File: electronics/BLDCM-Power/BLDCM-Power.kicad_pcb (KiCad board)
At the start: 4 copper layers, 32 x 32 mm, 37 parts, among them J1 501920-3001, J2 53048-0310, J3 53261-0471, J4 53261-0471, J5 FTSH-107-01-L-DV-K, J6 12402012E212A, U1 INA239-Q1, U2 LDL212PV33R, U3 TMC6300-LA, U4 INA239-Q1, U5 TCAN1462, U6 INA239-Q1

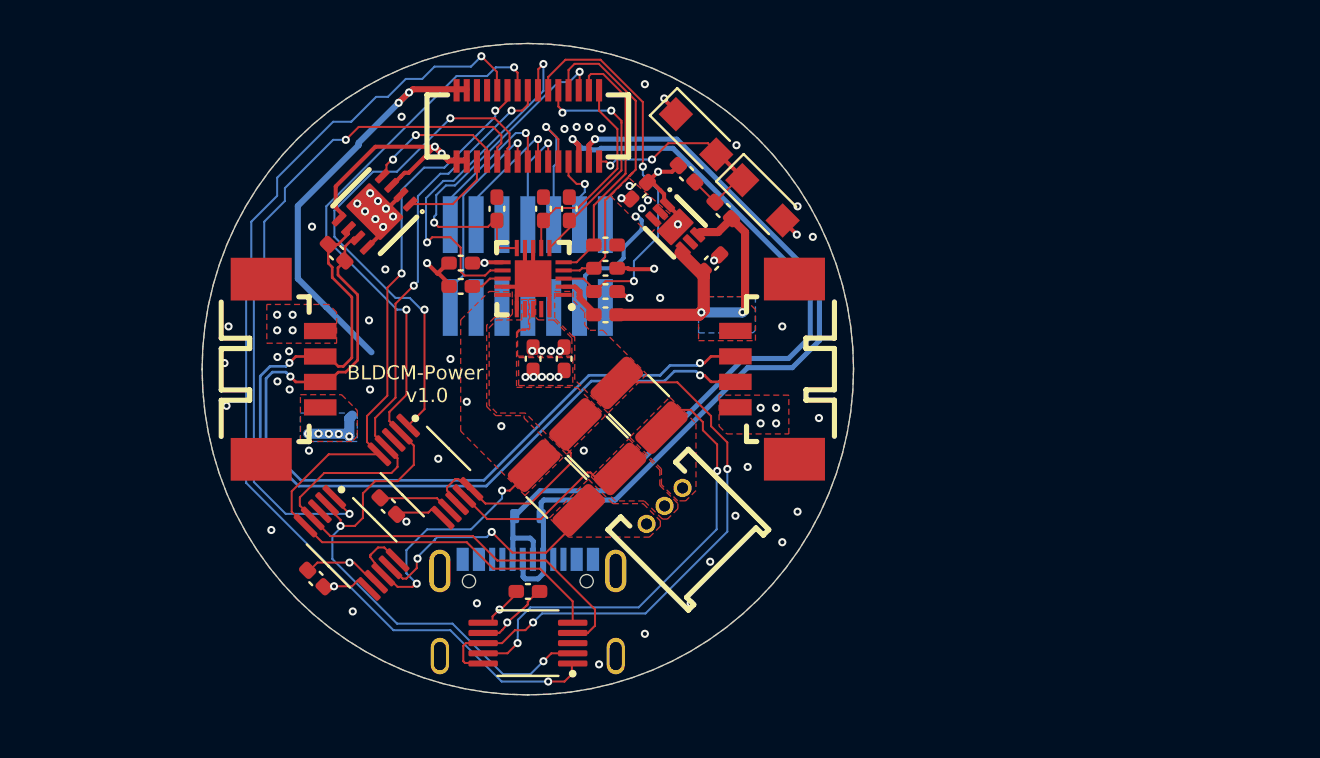
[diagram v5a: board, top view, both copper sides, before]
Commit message: Feat(schematic): Automatic power source selection
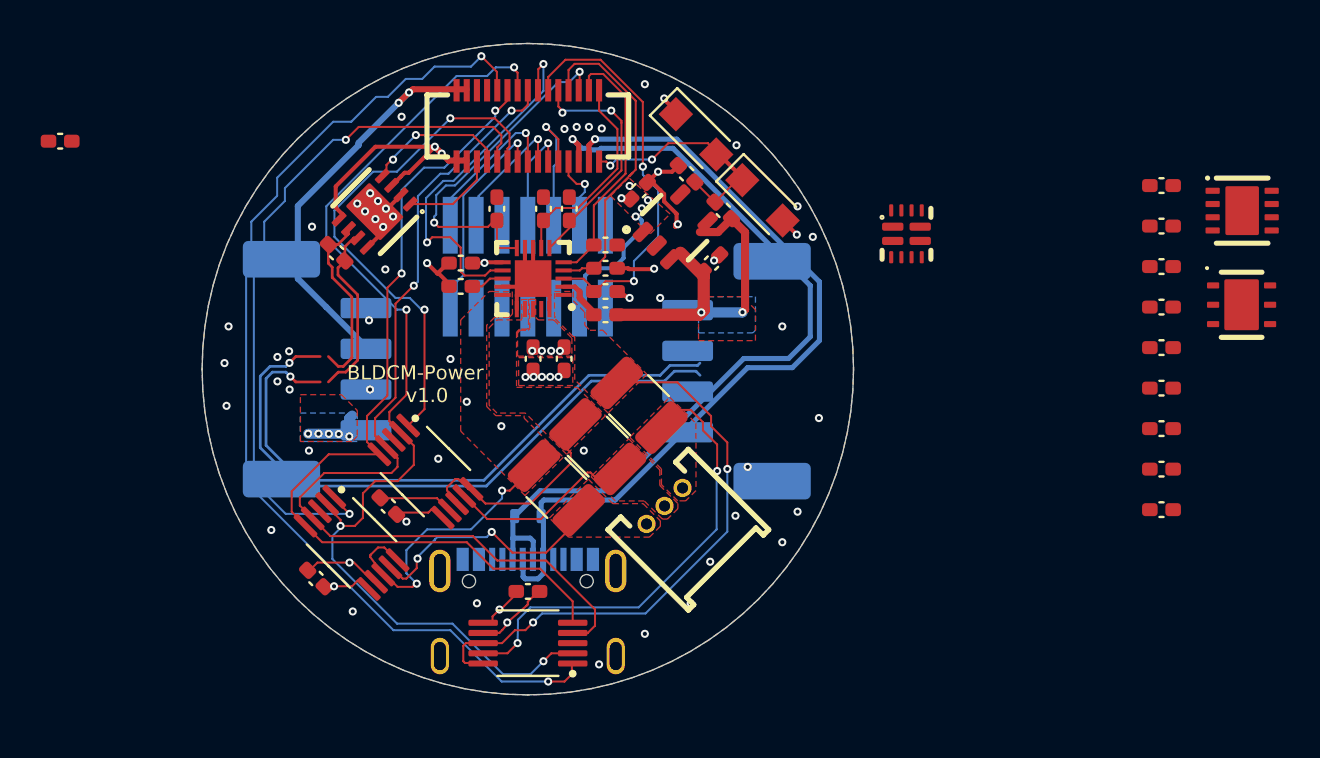
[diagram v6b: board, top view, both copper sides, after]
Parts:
- added C11: 1uF, BrenoCQ:C_0402, F.Cu at (179.6, 96.0)
- added C12: 1uF, BrenoCQ:C_0402, F.Cu at (179.6, 98.0)
- added C13: 100nF, BrenoCQ:C_0402, F.Cu at (179.6, 100.0)
- added C14: 100nF, BrenoCQ:C_0402, F.Cu at (179.6, 102.0)
- added R14: 100K, BrenoCQ:R_0402, F.Cu at (179.6, 103.9)
- added R15: 500, BrenoCQ:R_0402, F.Cu at (179.6, 105.9)
- added R16: 100K, BrenoCQ:R_0402, F.Cu at (179.6, 107.9)
- added R17: 100K, BrenoCQ:R_0402, F.Cu at (179.6, 109.9)
- added R18: 100K, BrenoCQ:R_0402, F.Cu at (179.6, 111.9)
- added R3: 5.1K, BrenoCQ:R_0402, F.Cu at (125.5, 93.8)
- added U7: TPS2121, BrenoCQ:VQFN-HR-12, F.Cu at (167.1, 98.4)
- added U8: LDO40LPU50RY, BrenoCQ:DFN-6-3x3, F.Cu at (183.6, 101.8)
- added U9: TPS2115ADRB, BrenoCQ:VSON-8, F.Cu at (183.6, 97.2)
- C4: value 4.7uF -> 1uF
- J3, J4: value 53261-0471 -> 505578-0460; footprint BrenoCQ:53261-0471 -> BrenoCQ:505578-0460; moved to B.Cu
- U2: value LDL212PV33R -> LDLN030G33R; footprint BrenoCQ:DFN-6-2x2 -> BrenoCQ:TSOT-23-5
- moved J3 1.10 mm to (136.4, 105.0), turned to -90 degrees
- moved J4 1.00 mm to (160.5, 105.1), turned to 90 degrees
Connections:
- C3 pad 2: VIN -> 5V
- J1 pad 2: VIN -> 5V
- J1 pad 4: VIN -> 5V
- J3 pad 1: VIN -> /CAN.DP
- J3 pad 2: /CAN.DP -> /CAN.DN
- J3 pad 3: /CAN.DN -> VIN
- J4 pad 1: VIN -> /CAN.DP
- J4 pad 2: /CAN.DP -> /CAN.DN
- J4 pad 3: /CAN.DN -> VIN
- J6 pad A4_B9: unconnected-(J6-VBUS-PadA4_B9) -> VBUS
- J6 pad A5: unconnected-(J6-CC1-PadA5) -> Net-(J6-CC1)
- J6 pad B4_A9: unconnected-(J6-VBUS-PadB4_A9) -> VBUS
- U2 pad 1: GND -> 5V
- U2 pad 2: 3.3V -> GND
- U2 pad 3: 3.3V -> 5V
- U2 pad 4: VIN -> Net-(U2-PG)
- U2 pad 5: unconnected-(U2-NC-Pad5) -> 3.3V
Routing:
- net /CAN.DN: track 42.6 -> 9.04 mm, vias 2 -> 0
- net VIN: track 61.4 -> 93.1 mm, vias 13 -> 14
- net /CAN.DP: track 41.4 -> 39.5 mm, vias 2 -> 1
- net unconnected-(J5-NC-Pad9): vias 0 -> 1
- net unconnected-(J4-PadMP1): vias 0 -> 1
- net GND: vias 70 -> 59
- net /VCP.RX: vias 1 -> 2

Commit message: Feat(schematic): Update volt sense to use BAT54S
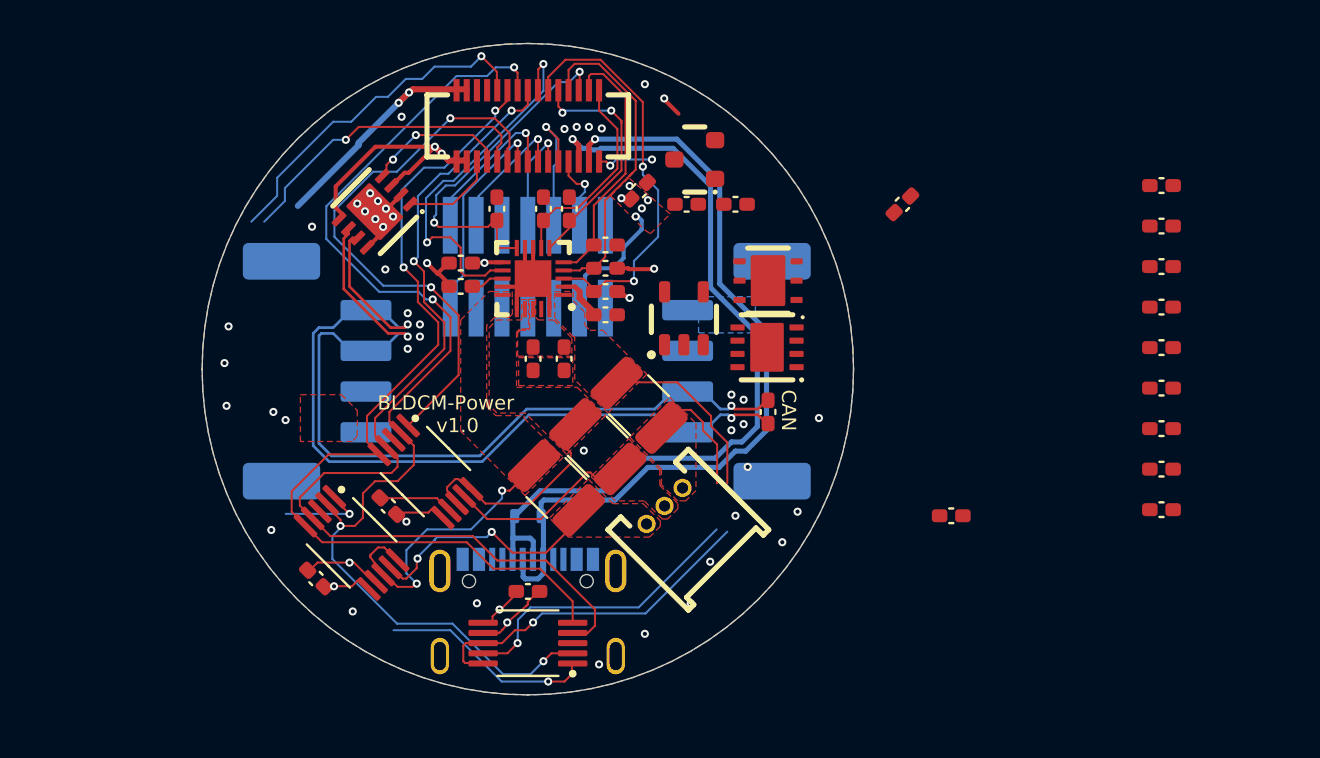
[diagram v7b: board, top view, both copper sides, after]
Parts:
- removed D1, D2: B0520LW, BrenoCQ:SOD-123
- U7: value TPS2121 -> BAT54S; footprint BrenoCQ:VQFN-HR-12 -> BrenoCQ:SOT-23
- moved R3 47.5 mm to (169.3, 112.2)
- moved U9 24.3 mm to (160.3, 103.9), turned to 180 degrees
- moved U8 23.3 mm to (160.3, 100.7), turned to 180 degrees
- moved R11 22.6 mm to (160.3, 107.1), turned to 90 degrees
- moved U7 11.0 mm to (156.7, 94.7), turned to 180 degrees
- moved C3 9.81 mm to (166.9, 96.9)
- moved U2 4.51 mm to (156.2, 102.5), turned to 0 degrees
- moved R13 2.83 mm to (158.7, 96.9), turned to 0 degrees
- moved R1 1.82 mm to (156.3, 96.9), turned to 0 degrees
- moved J3 0.10 mm to (136.4, 105.1)
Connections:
- U7 pad 1: Net-(U7-OUT-Pad1) -> GND
- U7 pad 2: unconnected-(U7-IN2-Pad2) -> 3.3V
- U7 pad 3: unconnected-(U7-CP2-Pad3) -> /VOLT
- U8 pad PAD: (no net) -> GND
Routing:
- net VIN: track 93.1 -> 16.6 mm, vias 14 -> 0
- net /CAN.DN: track 9.04 -> 41.9 mm, vias 0 -> 2
- net /INA.CS2: track 50.8 -> 27.7 mm
- net /INA.CS0: track 34.9 -> 19.7 mm
- net 5V: track 0.00 -> 11.5 mm, vias 0 -> 2
- net /VOLT: track 11.6 -> 2.81 mm
- net GND: track 35.1 -> 29.7 mm, vias 59 -> 47
- net /INA.PICO: track 51.9 -> 54.7 mm
- net /CAN.DP: track 39.5 -> 42.2 mm, vias 1 -> 2
- net /TMC.W.IN: track 28.4 -> 26.0 mm, vias 2 -> 1
- net /TMC.W.OUT: track 22.9 -> 20.6 mm, vias 2 -> 1
- net /INA.CS1: track 25.4 -> 27.6 mm
- net /INA.CLK: track 43.9 -> 45.4 mm
- net /INA.POCI: track 47.1 -> 48.3 mm
- net /USB.DP: track 40.6 -> 39.5 mm
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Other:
- board text added: "CAN"

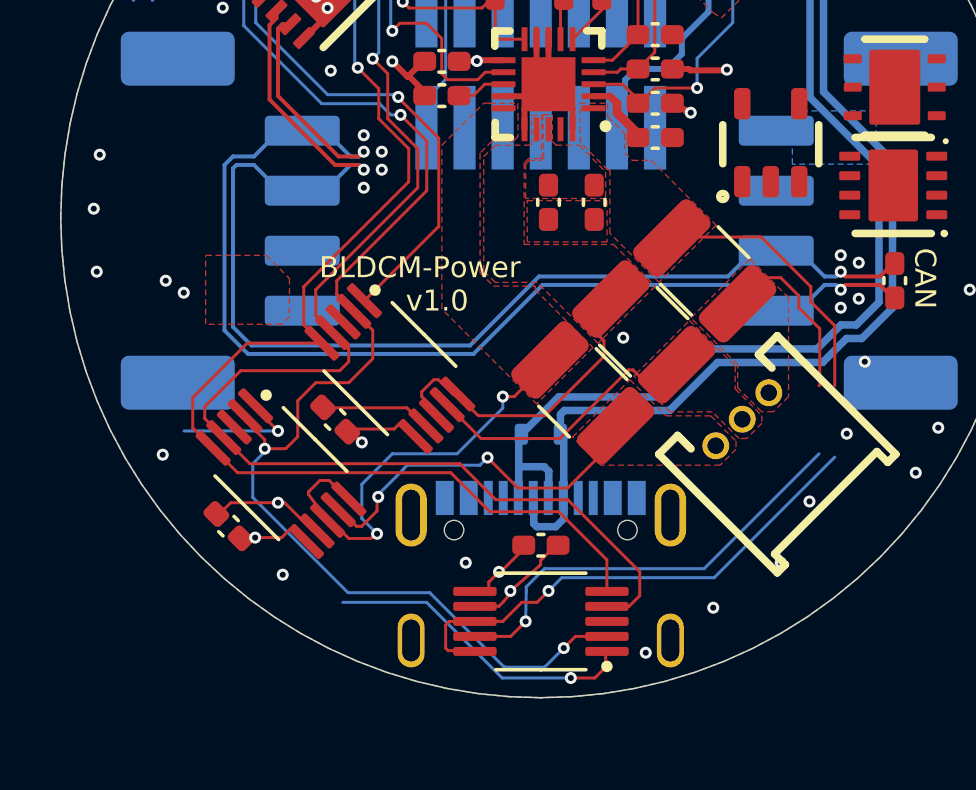
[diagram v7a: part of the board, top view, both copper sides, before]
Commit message: Feat(schematic): Replace INA239 with INA240
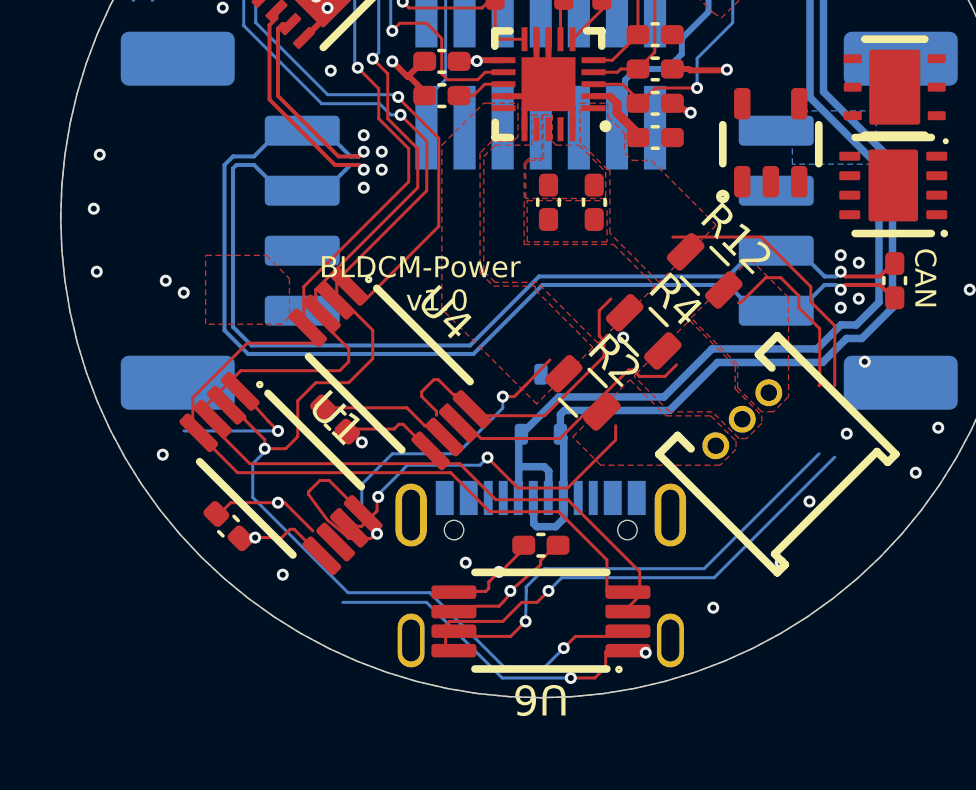
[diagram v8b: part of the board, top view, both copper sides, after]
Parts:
- R12, R2, R4: value 150m -> KRL1220 50m; footprint BrenoCQ:R_1210 -> BrenoCQ:KRL1220
- U1, U4, U6: value INA239-Q1 -> INA240A1PWR; footprint BrenoCQ:VSSOP-10 -> BrenoCQ:TSSOP-8
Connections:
- R1 pad 1: VIN -> /VOLT
- R1 pad 2: /VOLT -> VIN
- R10 pad 1: /TMC.WL -> GND
- R10 pad 2: GND -> /TMC.WL
- R11 pad 1: /CAN.DP -> /CAN.DN
- R11 pad 2: /CAN.DN -> /CAN.DP
- R13 pad 1: /VOLT -> GND
- R13 pad 2: GND -> /VOLT
- R14 pad 1: Net-(U2-PG) -> 3.3V
- R14 pad 2: 3.3V -> Net-(U2-PG)
- R15 pad 1: GND -> Net-(U9-ILIM)
- R15 pad 2: Net-(U9-ILIM) -> GND
- R16 pad 1: GND -> VIN
- R16 pad 2: VIN -> GND
- R17 pad 1: GND -> VBUS
- R17 pad 2: VBUS -> GND
- R18 pad 1: GND -> Net-(U8-SENSE)
- R18 pad 2: Net-(U8-SENSE) -> GND
- R3 pad 1: Net-(J6-CC1) -> GND
- R3 pad 2: GND -> Net-(J6-CC1)
- R5 pad 1: /TMC.UH -> GND
- R5 pad 2: GND -> /TMC.UH
- R6 pad 1: /TMC.UL -> GND
- R6 pad 2: GND -> /TMC.UL
- R7 pad 1: /TMC.VH -> GND
- R7 pad 2: GND -> /TMC.VH
- R8 pad 1: /TMC.VL -> GND
- R8 pad 2: GND -> /TMC.VL
- R9 pad 1: /TMC.WH -> GND
- R9 pad 2: GND -> /TMC.WH
- U1 pad 1: /INA.CS0 -> unconnected-(U1-NC-Pad1)
- U1 pad 2: /INA.PICO -> /TMC.U.OUT
- U1 pad 3: unconnected-(U1-ALERT-Pad3) -> /TMC.U.IN
- U1 pad 4: /INA.POCI -> GND
- U1 pad 5: /INA.CLK -> 3.3V
- U1 pad 8: /TMC.U.IN -> /INA.U
- U4 pad 1: /INA.CS1 -> unconnected-(U4-NC-Pad1)
- U4 pad 2: /INA.PICO -> /TMC.V.OUT
- U4 pad 3: unconnected-(U4-ALERT-Pad3) -> /TMC.V.IN
- U4 pad 4: /INA.POCI -> GND
- U4 pad 5: /INA.CLK -> 3.3V
- U4 pad 8: /TMC.V.IN -> /INA.V
- U6 pad 1: /INA.CS2 -> unconnected-(U6-NC-Pad1)
- U6 pad 2: /INA.PICO -> /TMC.W.OUT
- U6 pad 3: unconnected-(U6-ALERT-Pad3) -> /TMC.W.IN
- U6 pad 4: /INA.POCI -> GND
- U6 pad 5: /INA.CLK -> 3.3V
- U6 pad 8: /TMC.W.IN -> /INA.W
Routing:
- net /TMC.V.IN: track 10.7 -> 0.00 mm
- net /INA.V: track 0.00 -> 10.7 mm
- net /INA.CS2: track 27.7 -> 17.1 mm, vias 2 -> 1
- net unconnected-(U6-NC-Pad1): track 0.00 -> 10.5 mm, vias 0 -> 2
- net GND: track 29.7 -> 27.0 mm, vias 47 -> 44
- net /TMC.VH: track 16.5 -> 18.5 mm, vias 0 -> 1
- net /TMC.UH: track 20.1 -> 20.9 mm, vias 2 -> 3
